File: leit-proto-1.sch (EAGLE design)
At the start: 31 parts, among them J3 FTDI_DEVICE, J4 C-GRID-02-70553, J5 C-GRID-02-70553, J6 C-GRID-02-70553, J7 C-GRID-02-70553, J8 C-GRID-02-70553, J9 M25PTH, Q1 CSD17551Q3A, Q2 CSD17551Q3A, Q3 CSD17551Q3A, Q4 CSD17551Q3A, U1 R-78E5.0-0.5, U2 IR4427S, U3 IR4427S

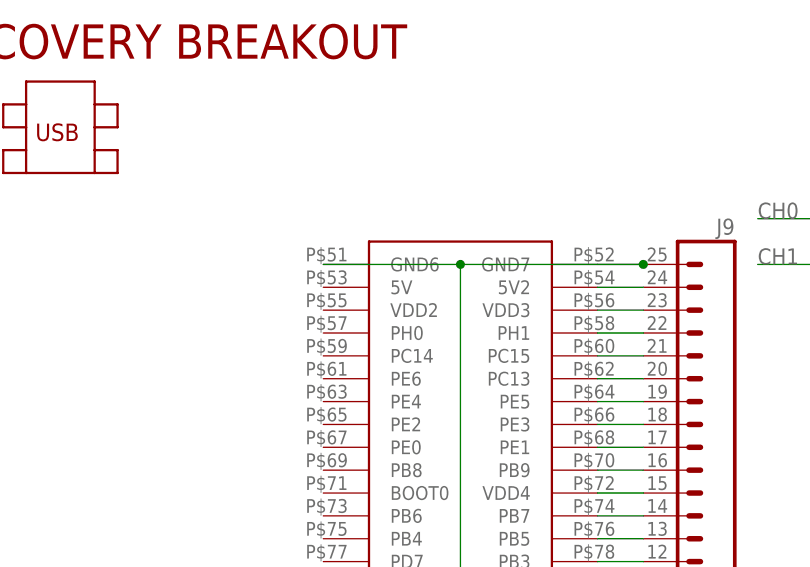
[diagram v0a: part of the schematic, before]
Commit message: PCB layout complete for barebones proto
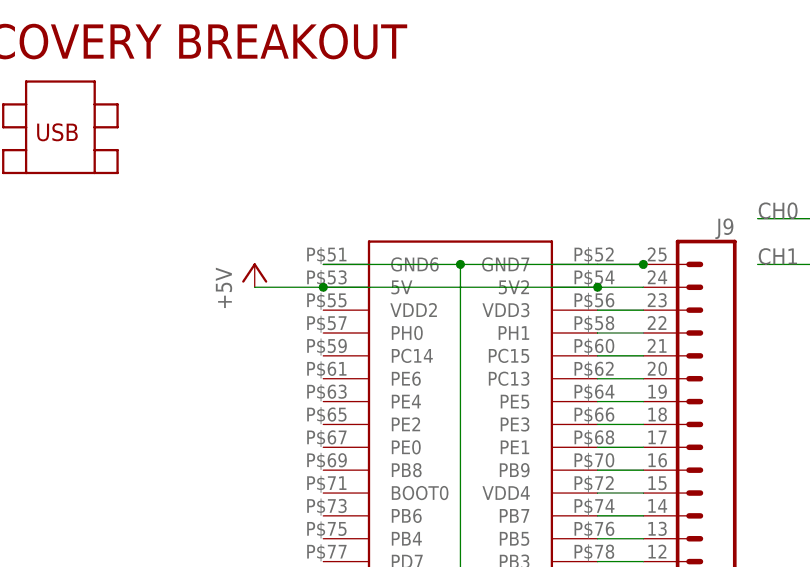
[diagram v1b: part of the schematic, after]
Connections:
- removed net N$31: J9.24, MOD1.5V2
- net +5V: now also J9.24, MOD1.5V, MOD1.5V2
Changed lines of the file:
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@@
 <?xml version="1.0" encoding="utf-8"?>
 <!DOCTYPE eagle SYSTEM "eagle.dtd">
-<eagle version="6.4">
+<eagle version="6.3">
 <drawing>
 <settings>
@@
 <part name="P+9" library="supply1" deviceset="+12V" device=""/>
 <part name="J9" library="SparkFun-Connectors" deviceset="M25" device="PTH"/>
+<part name="P+10" library="supply1" deviceset="+5V" device=""/>
 </parts>
 <sheets>
@@
 <instance part="P+9" gate="1" x="-63.5" y="-73.66"/>
 <instance part="J9" gate="G$1" x="-2.54" y="-15.24" rot="MR0"/>
+<instance part="P+10" gate="1" x="-55.88" y="15.24"/>
 </instances>
 <busses>
@@
 <junction x="86.36" y="-83.82"/>
 </segment>
+<segment>
+<pinref part="P+10" gate="1" pin="+5V"/>
+<pinref part="MOD1" gate="G$1" pin="5V"/>
+<wire x1="-55.88" y1="12.7" x2="-48.26" y2="12.7" width="0.1524" layer="91"/>
+<pinref part="MOD1" gate="G$1" pin="5V2"/>
+<pinref part="J9" gate="G$1" pin="24"/>
+<wire x1="-12.7" y1="12.7" x2="-17.78" y2="12.7" width="0.1524" layer="91"/>
+<wire x1="-48.26" y1="12.7" x2="-17.78" y2="12.7" width="0.1524" layer="91"/>
+<junction x="-48.26" y="12.7"/>
+<junction x="-17.78" y="12.7"/>
+</segment>
 </net>
 <net name="CH0_L" class="0">
@@
 </segment>
 </net>
-<net name="N$31" class="0">
-<segment>
-<pinref part="MOD1" gate="G$1" pin="5V2"/>
-<pinref part="J9" gate="G$1" pin="24"/>
-<wire x1="-12.7" y1="12.7" x2="-17.78" y2="12.7" width="0.1524" layer="91"/>
-</segment>
-</net>
